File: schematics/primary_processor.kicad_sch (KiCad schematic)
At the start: 15 parts

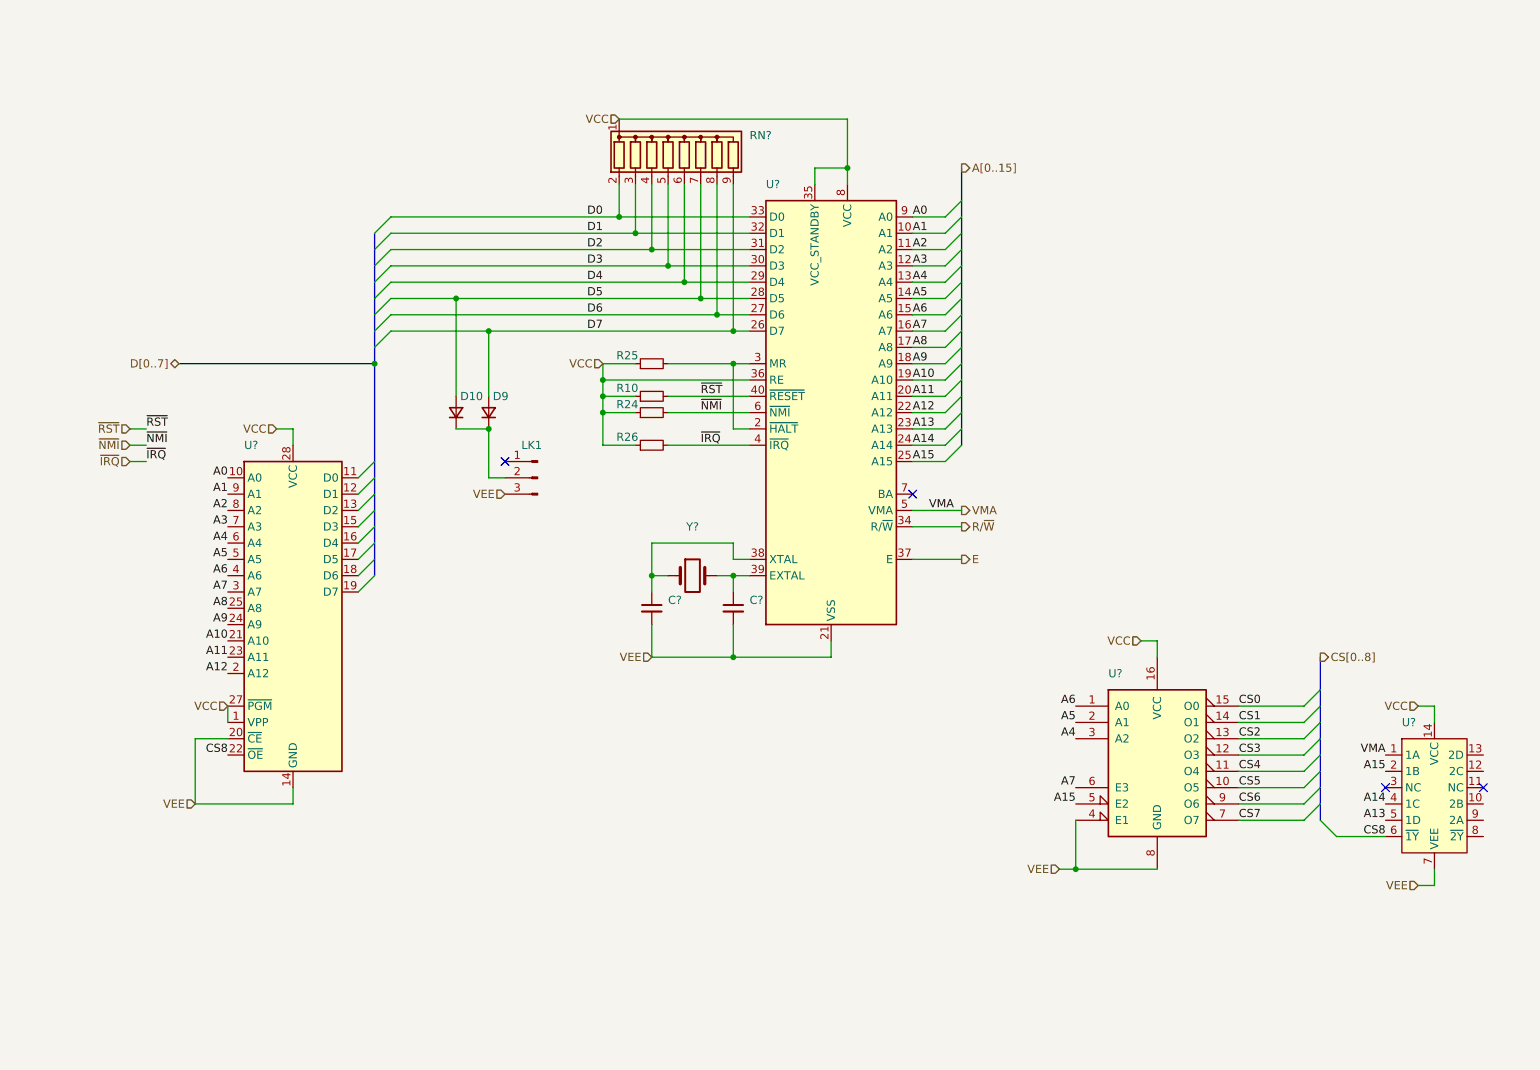
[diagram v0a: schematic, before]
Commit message: Moved more components into hierachical sheets, misc cleanup
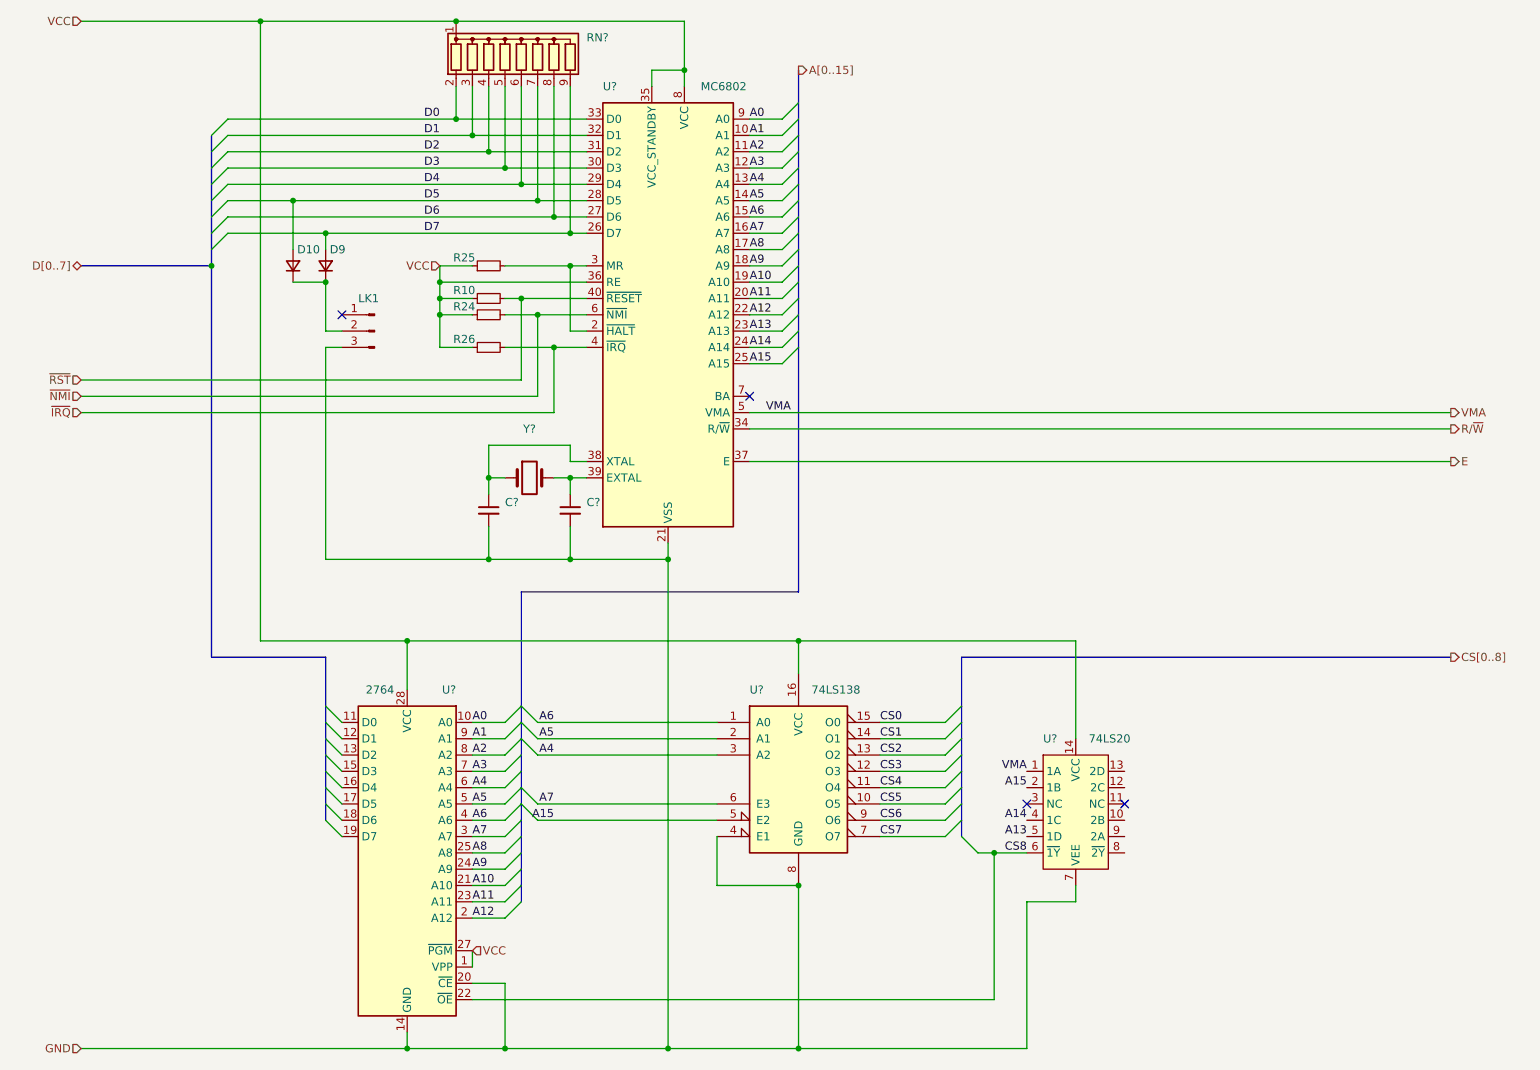
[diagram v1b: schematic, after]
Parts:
- removed U?: ~, symbol Memory_EPROM:2764
- removed U?: ~, symbol 74xx:74LS138
- removed U?: ~, symbol Custom:74LS20
- added U?: 74LS138, symbol 74xx:74LS138
- added U?: 74LS20, symbol Custom:74LS20
- added U?: 2764, symbol Memory_EPROM:2764
- U?: value ~ -> MC6802
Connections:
- net A0: now also U?.10 (A0)
- net A1: now also U?.9 (A1)
- net A10: now also U?.21 (A10)
- net A11: now also U?.23 (A11)
- net A12: now also U?.2 (A12)
- net A13: now also U?.5 (1D)
- net A14: now also U?.4 (1C)
- net A15: now also U?.2 (1B), U?.5 (E2)
- net A2: now also U?.8 (A2)
- net A3: now also U?.7 (A3)
- net A4: now also U?.3 (A2), U?.6 (A4)
- net A5: now also U?.2 (A1), U?.5 (A5)
- net A6: now also U?.1 (A0), U?.4 (A6)
- net A7: now also U?.3 (A7), U?.6 (E3)
- net A8: now also U?.25 (A8)
- net A9: now also U?.24 (A9)
- net CS0: now also U?.15 (O0)
- net CS1: now also U?.14 (O1)
- net CS2: now also U?.13 (O2)
- net CS3: now also U?.12 (O3)
- net CS4: now also U?.11 (O4)
- net CS5: now also U?.10 (O5)
- net CS6: now also U?.9 (O6)
- net CS7: now also U?.7 (O7)
- net CS8: now also U?.22 (~{OE}), U?.6 (~{1Y})
- net VCC: now also U?.1 (VPP), U?.14 (VCC), U?.16 (VCC), U?.27 (~{PGM}), U?.28 (VCC)
- net VMA: now also U?.1 (1A)
- net VEE renamed GND
- net GND: now also U?.14 (GND), U?.20 (~{CE}), U?.4 (E1), U?.7 (VEE), U?.8 (GND)
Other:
- moved on the sheet: C?, D10, D9, LK1, R10, R24, R25, R26, RN?, U?, Y?

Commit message: cleanup, fixes, started on power supplies
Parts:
- added C16, C27, C28, C29: 0u1, symbol Device:C_Small
- C30, C31: renamed from C?; value ~ -> 27p
- IC14: renamed from U?; footprint (none) -> Package_DIP:DIP-28_W15.24mm
- IC24: renamed from U?; footprint (none) -> Package_DIP:DIP-40_W15.24mm
- RP4: renamed from RN?; footprint (none) -> Resistor_THT:R_Array_SIP9
- gave numbers to parts that had none: 3
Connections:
- net GND: now also C16.2, C27.2, C28.2, C29.2
- net VCC: now also C16.1, C27.1, C28.1, C29.1
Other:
- moved on the sheet: C30, C31, X2

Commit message: More power supply work
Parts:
- IC22: value 74LS138 -> 74LD138
- IC23: value 74LS20 -> 74LD20

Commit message: Updated to KiCad v10.0. Minor improvements.
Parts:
- D10, D9, LK1, R10, R24, R25, R26, RP4, X2: value ~ -> (none)
